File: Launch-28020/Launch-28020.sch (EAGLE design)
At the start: 24 parts, among them U1 3.3V

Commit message: Updated Schematic
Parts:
- removed C2, C3, C4, C5, C6: (no value), rcl:C-USC1206
- removed R4, R6, R7: (no value), resistor:R-US_M1206
- added QF1: 8M10AHC49T, crystal:8M10AHC49T
- R1: value (none) -> 2k2
- R2, R3: value (none) -> 56k
- R8, R9: value (none) -> 4k7
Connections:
- new net N$12: R3.2, U$1.GPIO34
- new net N$6: C8.2, QF1.1, U$1.X1
- new net N$7: C1.2, QF1.3, U$1.X2
- new net N$8: J3.14, R9.1
- new net N$9: J3.13, R8.2
- new net TRST: J3.2, R1.1, U$1.TRST
- net GND: now also C1.1, C8.1, C9.2, J3.10, J3.12, J3.4, J3.8, R1.2, U1.NC
- net TCK: now also J3.11
- net TDI: now also J3.3
- net TDO: now also J3.7, R2.2
- net TMS: now also J3.1
- net VDD: now also C9.1, J3.5, R2.1, R3.1, R8.1, R9.2, U1.OUT
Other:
- moved on the sheet: C1, C11, C8, C9, J3, R1, R2, R3, R8, R9

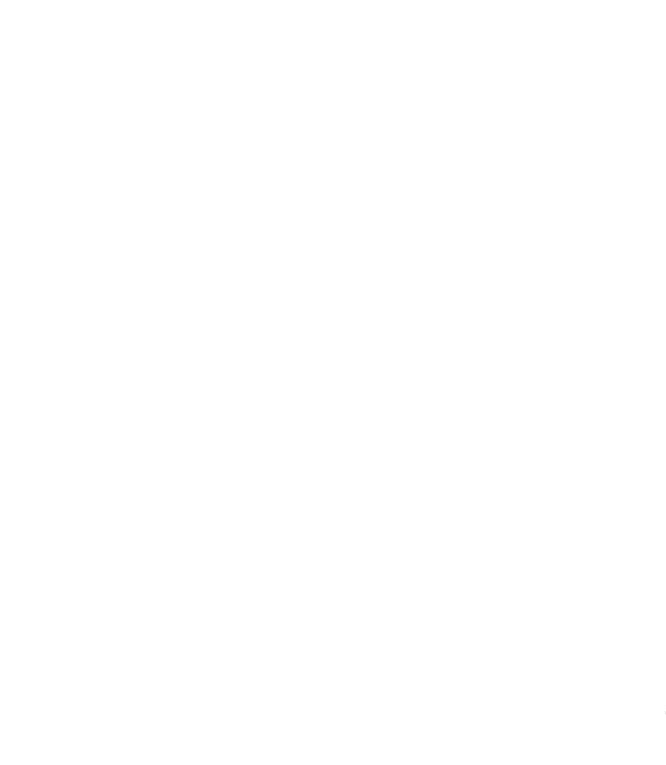
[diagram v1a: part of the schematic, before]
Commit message: Added IO headeres
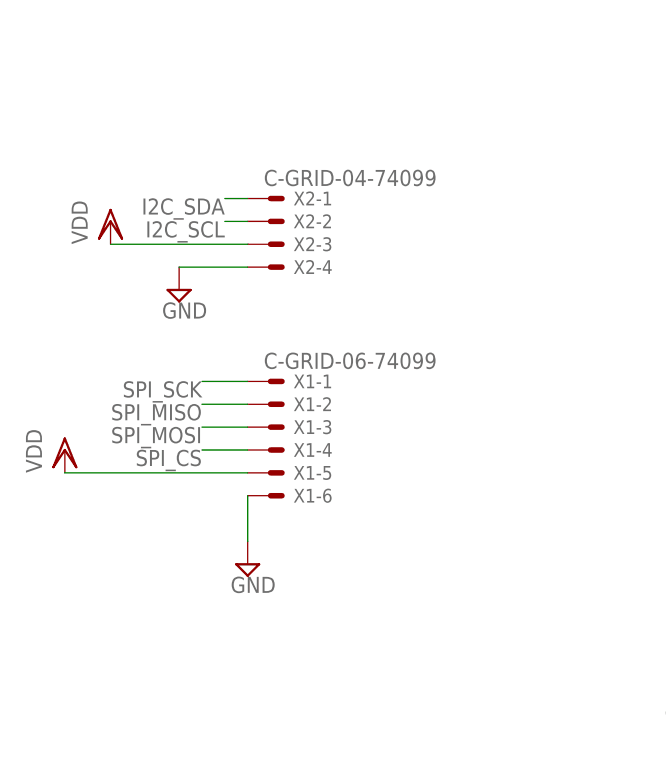
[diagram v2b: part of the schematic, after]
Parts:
- added X1: C-GRID-06-74099, con-molex:C-GRID-06-74099
- added X2: C-GRID-04-74099, con-molex:C-GRID-04-74099
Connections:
- new net I2C_SCL: X2-2.S
- new net I2C_SDA: X2-1.S
- new net SPI_CS: X1-4.S
- new net SPI_MISO: X1-2.S
- new net SPI_MOSI: X1-3.S
- new net SPI_SCK: X1-1.S
- net GND: now also X1-6.S, X2-4.S
- net VDD: now also X1-5.S, X2-3.S
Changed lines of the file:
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@@
 <part name="VDD6" library="supply1" library_urn="urn:adsk.eagle:library:371" deviceset="VDD" device=""/>
 <part name="VDD7" library="supply1" library_urn="urn:adsk.eagle:library:371" deviceset="VDD" device=""/>
+<part name="X1" library="con-molex" library_urn="urn:adsk.eagle:library:165" deviceset="C-GRID-06" device="-74099"/>
+<part name="SUPPLY6" library="supply2" library_urn="urn:adsk.eagle:library:372" deviceset="GND" device=""/>
+<part name="VDD8" library="supply1" library_urn="urn:adsk.eagle:library:371" deviceset="VDD" device=""/>
+<part name="X2" library="con-molex" library_urn="urn:adsk.eagle:library:165" deviceset="C-GRID-04" device="-74099"/>
+<part name="VDD9" library="supply1" library_urn="urn:adsk.eagle:library:371" deviceset="VDD" device=""/>
+<part name="SUPPLY10" library="supply2" library_urn="urn:adsk.eagle:library:372" deviceset="GND" device=""/>
 </parts>
 <sheets>
@@
 <instance part="VDD6" gate="G$1" x="121.92" y="78.74"/>
 <instance part="VDD7" gate="G$1" x="-60.96" y="-33.02" rot="R180"/>
+<instance part="X1" gate="-1" x="-106.68" y="63.5"/>
+<instance part="X1" gate="-2" x="-106.68" y="60.96"/>
+<instance part="X1" gate="-3" x="-106.68" y="58.42"/>
+<instance part="X1" gate="-4" x="-106.68" y="55.88"/>
+<instance part="X1" gate="-5" x="-106.68" y="53.34"/>
+<instance part="X1" gate="-6" x="-106.68" y="50.8"/>
+<instance part="SUPPLY6" gate="GND" x="-109.22" y="43.18"/>
+<instance part="VDD8" gate="G$1" x="-129.54" y="55.88"/>
+<instance part="X2" gate="-1" x="-106.68" y="83.82"/>
+<instance part="X2" gate="-2" x="-106.68" y="81.28"/>
+<instance part="X2" gate="-3" x="-106.68" y="78.74"/>
+<instance part="X2" gate="-4" x="-106.68" y="76.2"/>
+<instance part="VDD9" gate="G$1" x="-124.46" y="81.28"/>
+<instance part="SUPPLY10" gate="GND" x="-116.84" y="73.66"/>
 </instances>
 <busses>
@@
 <wire x1="-60.96" y1="-25.4" x2="-48.26" y2="-25.4" width="0.1524" layer="91"/>
 <pinref part="VDD7" gate="G$1" pin="VDD"/>
+</segment>
+<segment>
+<pinref part="X1" gate="-5" pin="S"/>
+<pinref part="VDD8" gate="G$1" pin="VDD"/>
+<wire x1="-109.22" y1="53.34" x2="-129.54" y2="53.34" width="0.1524" layer="91"/>
+</segment>
+<segment>
+<pinref part="X2" gate="-3" pin="S"/>
+<pinref part="VDD9" gate="G$1" pin="VDD"/>
+<wire x1="-109.22" y1="78.74" x2="-124.46" y2="78.74" width="0.1524" layer="91"/>
 </segment>
 </net>
@@
 <wire x1="63.5" y1="-10.16" x2="63.5" y2="-7.62" width="0.1524" layer="91"/>
 </segment>
+<segment>
+<pinref part="SUPPLY6" gate="GND" pin="GND"/>
+<pinref part="X1" gate="-6" pin="S"/>
+<wire x1="-109.22" y1="45.72" x2="-109.22" y2="50.8" width="0.1524" layer="91"/>
+</segment>
+<segment>
+<pinref part="X2" gate="-4" pin="S"/>
+<pinref part="SUPPLY10" gate="GND" pin="GND"/>
+<wire x1="-109.22" y1="76.2" x2="-116.84" y2="76.2" width="0.1524" layer="91"/>
+</segment>
 </net>
 <net name="N$3" class="0">
@@
 </segment>
 </net>
+<net name="SPI_SCK" class="0">
+<segment>
+<pinref part="X1" gate="-1" pin="S"/>
+<wire x1="-109.22" y1="63.5" x2="-114.3" y2="63.5" width="0.1524" layer="91"/>
+<label x="-114.3" y="63.5" size="1.778" layer="95" rot="R180"/>
+</segment>
+</net>
+<net name="SPI_MISO" class="0">
+<segment>
+<pinref part="X1" gate="-2" pin="S"/>
+<wire x1="-109.22" y1="60.96" x2="-114.3" y2="60.96" width="0.1524" layer="91"/>
+<label x="-114.3" y="60.96" size="1.778" layer="95" rot="R180"/>
+</segment>
+</net>
+<net name="SPI_MOSI" class="0">
+<segment>
+<pinref part="X1" gate="-3" pin="S"/>
+<wire x1="-109.22" y1="58.42" x2="-114.3" y2="58.42" width="0.1524" layer="91"/>
+<label x="-114.3" y="58.42" size="1.778" layer="95" rot="R180"/>
+</segment>
+</net>
+<net name="SPI_CS" class="0">
+<segment>
+<pinref part="X1" gate="-4" pin="S"/>
+<wire x1="-109.22" y1="55.88" x2="-114.3" y2="55.88" width="0.1524" layer="91"/>
+<label x="-114.3" y="55.88" size="1.778" layer="95" rot="R180"/>
+</segment>
+</net>
+<net name="I2C_SDA" class="0">
+<segment>
+<pinref part="X2" gate="-1" pin="S"/>
+<wire x1="-109.22" y1="83.82" x2="-111.76" y2="83.82" width="0.1524" layer="91"/>
+<label x="-111.76" y="83.82" size="1.778" layer="95" rot="R180"/>
+</segment>
+</net>
+<net name="I2C_SCL" class="0">
+<segment>
+<pinref part="X2" gate="-2" pin="S"/>
+<wire x1="-109.22" y1="81.28" x2="-111.76" y2="81.28" width="0.1524" layer="91"/>
+<label x="-111.76" y="81.28" size="1.778" layer="95" rot="R180"/>
+</segment>
+</net>

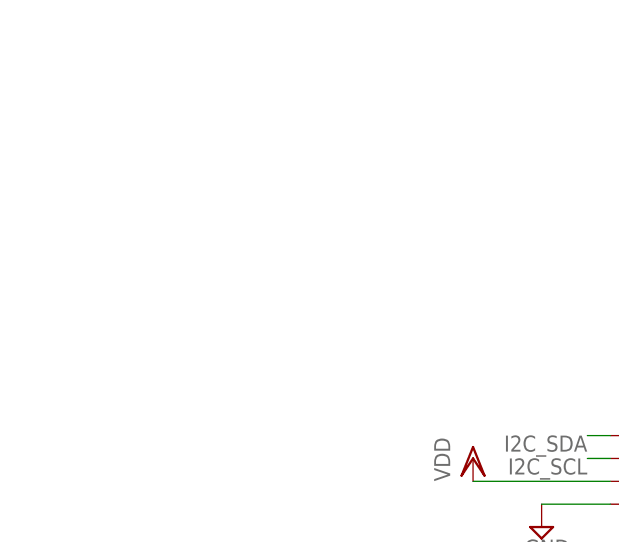
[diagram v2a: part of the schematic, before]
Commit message: Updated the schematic to include power circuitry and connectivity.
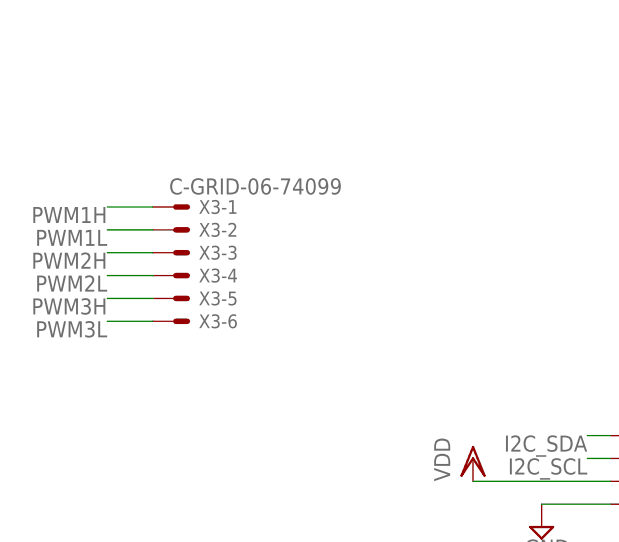
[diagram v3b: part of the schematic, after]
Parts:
- added X3: C-GRID-06-74099, con-molex:C-GRID-06-74099
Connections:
- new net PWM1H: X3-1.S
- new net PWM1L: X3-2.S
- new net PWM2H: X3-3.S
- new net PWM2L: X3-4.S
- new net PWM3H: X3-5.S
- new net PWM3L: X3-6.S
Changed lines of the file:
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@@
 <part name="VDD9" library="supply1" library_urn="urn:adsk.eagle:library:371" deviceset="VDD" device=""/>
 <part name="SUPPLY10" library="supply2" library_urn="urn:adsk.eagle:library:372" deviceset="GND" device=""/>
+<part name="X3" library="con-molex" library_urn="urn:adsk.eagle:library:165" deviceset="C-GRID-06" device="-74099"/>
 </parts>
 <sheets>
@@
 <instance part="VDD9" gate="G$1" x="-124.46" y="81.28"/>
 <instance part="SUPPLY10" gate="GND" x="-116.84" y="73.66"/>
+<instance part="X3" gate="-1" x="-157.48" y="109.22"/>
+<instance part="X3" gate="-2" x="-157.48" y="106.68"/>
+<instance part="X3" gate="-3" x="-157.48" y="104.14"/>
+<instance part="X3" gate="-4" x="-157.48" y="101.6"/>
+<instance part="X3" gate="-5" x="-157.48" y="99.06"/>
+<instance part="X3" gate="-6" x="-157.48" y="96.52"/>
 </instances>
 <busses>
@@
 </segment>
 </net>
+<net name="PWM1H" class="0">
+<segment>
+<pinref part="X3" gate="-1" pin="S"/>
+<wire x1="-160.02" y1="109.22" x2="-165.1" y2="109.22" width="0.1524" layer="91"/>
+<label x="-165.1" y="109.22" size="1.778" layer="95" rot="R180"/>
+</segment>
+</net>
+<net name="PWM1L" class="0">
+<segment>
+<pinref part="X3" gate="-2" pin="S"/>
+<wire x1="-160.02" y1="106.68" x2="-165.1" y2="106.68" width="0.1524" layer="91"/>
+<label x="-165.1" y="106.68" size="1.778" layer="95" rot="R180"/>
+</segment>
+</net>
+<net name="PWM2H" class="0">
+<segment>
+<pinref part="X3" gate="-3" pin="S"/>
+<wire x1="-160.02" y1="104.14" x2="-165.1" y2="104.14" width="0.1524" layer="91"/>
+<label x="-165.1" y="104.14" size="1.778" layer="95" rot="R180"/>
+</segment>
+</net>
+<net name="PWM2L" class="0">
+<segment>
+<pinref part="X3" gate="-4" pin="S"/>
+<wire x1="-160.02" y1="101.6" x2="-165.1" y2="101.6" width="0.1524" layer="91"/>
+<label x="-165.1" y="101.6" size="1.778" layer="95" rot="R180"/>
+</segment>
+</net>
+<net name="PWM3H" class="0">
+<segment>
+<pinref part="X3" gate="-5" pin="S"/>
+<wire x1="-160.02" y1="99.06" x2="-165.1" y2="99.06" width="0.1524" layer="91"/>
+<label x="-165.1" y="99.06" size="1.778" layer="95" rot="R180"/>
+</segment>
+</net>
+<net name="PWM3L" class="0">
+<segment>
+<pinref part="X3" gate="-6" pin="S"/>
+<wire x1="-160.02" y1="96.52" x2="-165.1" y2="96.52" width="0.1524" layer="91"/>
+<label x="-165.1" y="96.52" size="1.778" layer="95" rot="R180"/>
+</segment>
+</net>

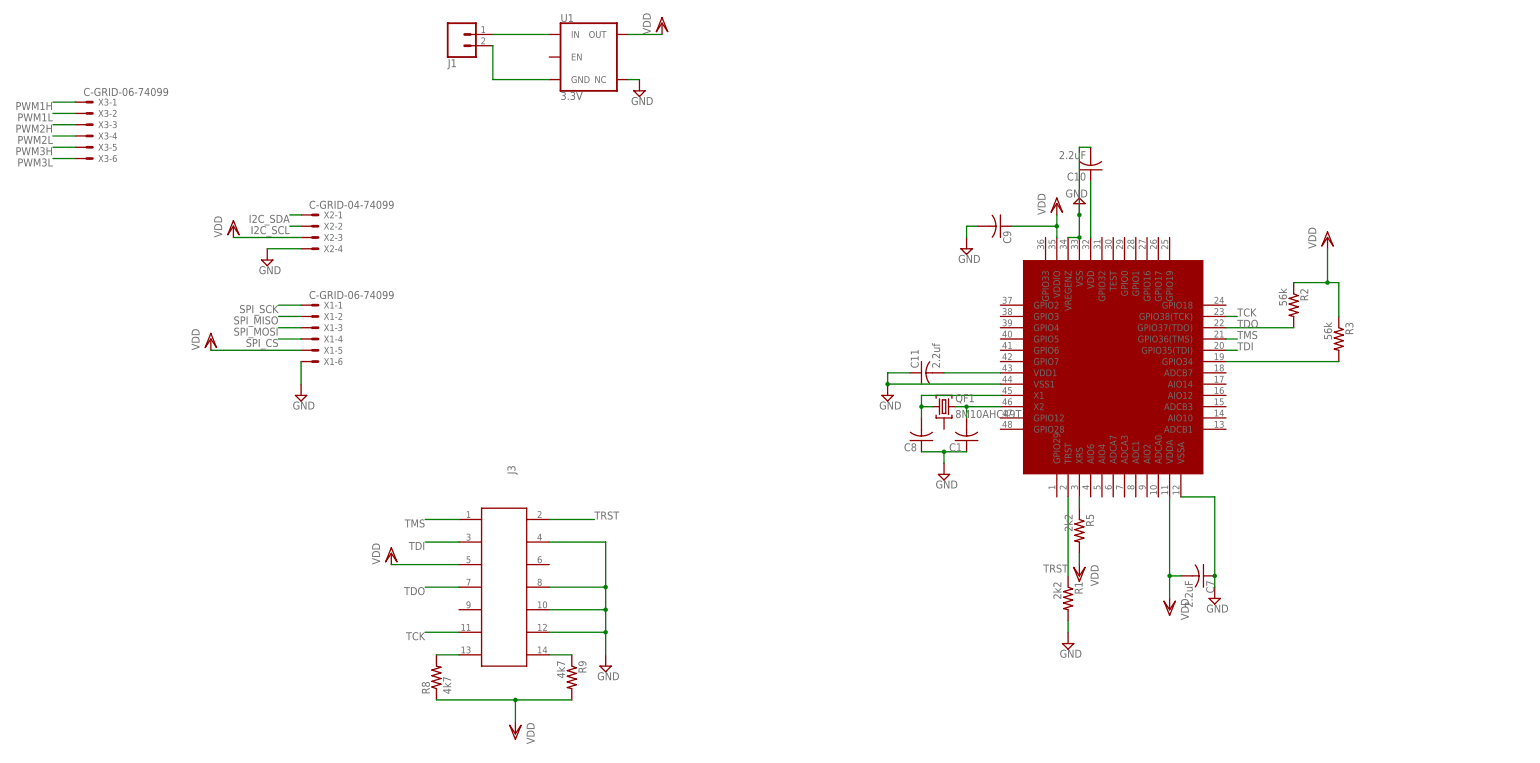
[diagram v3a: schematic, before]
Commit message: Created a working schematic and board layout. THe laytout can be optimized there seens to be some extra board space for the ground plane. Could also use mounting holes.
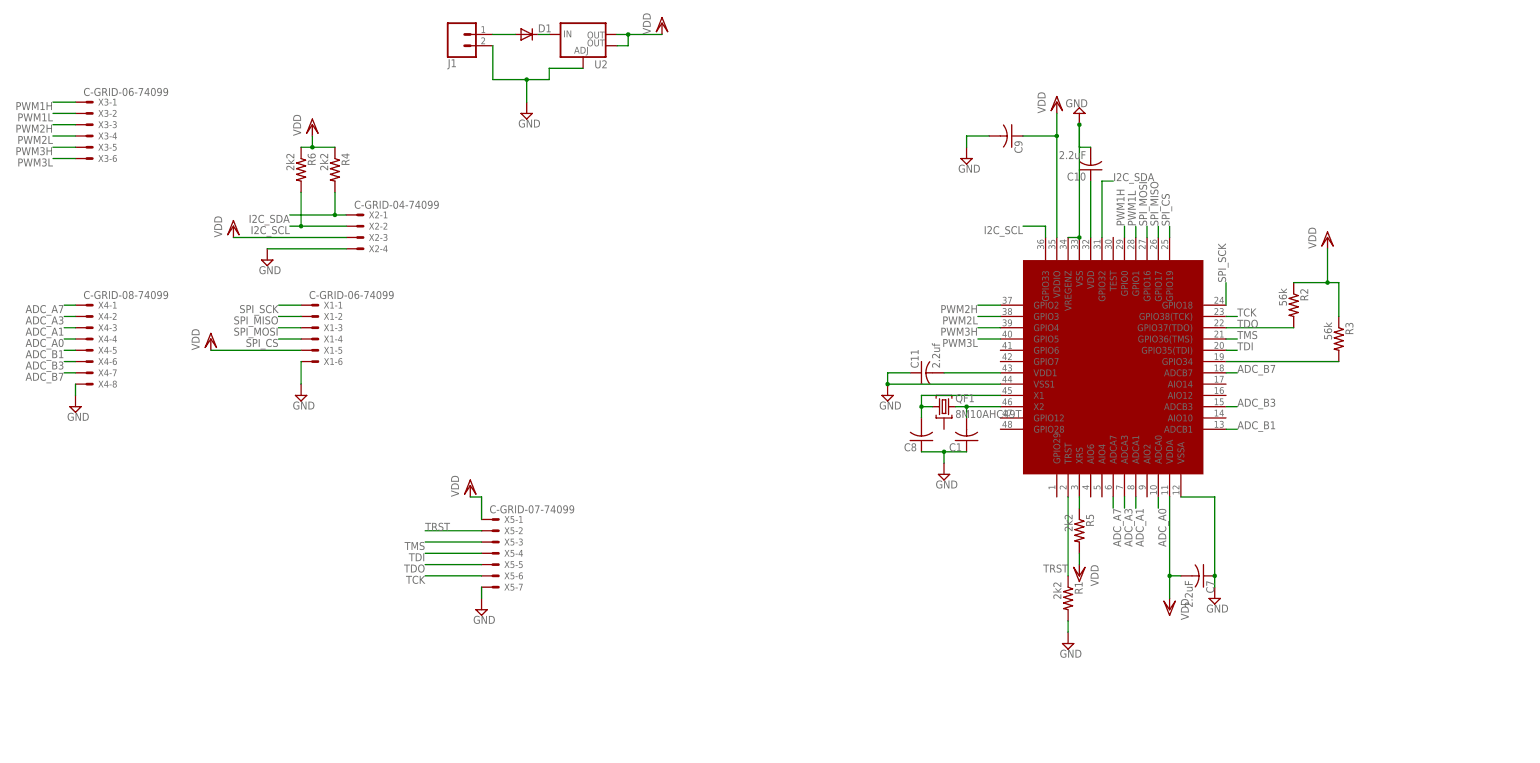
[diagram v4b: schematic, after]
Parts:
- removed J3: (no value), Wurth_Elektronik_Electromechanic_Wire_to_Board_Connectors_rev17b:61201422323
- removed R8, R9: 4k7, resistor:R-US_M1206
- removed U1: 3.3V, SparkFun-IC-Power:V_REG_AP2112K-3.3V
- added D1: (no value), diode:DIODE-SOD106-W
- added R4, R6: 2k2, resistor:R-US_M1206
- added U2: (no value), SparkFun-IC-Power:V_REG_LM1117SOT223
- added X4: C-GRID-08-74099, con-molex:C-GRID-08-74099
- added X5: C-GRID-07-74099, con-molex:C-GRID-07-74099
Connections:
- removed net N$2: J1.2, U1.GND
- removed net N$9: J3.13, R8.2
- new net ADC_A0: U$1.ADCA0, X4-4.S
- new net ADC_A1: U$1.ADCA1, X4-3.S
- new net ADC_A3: U$1.ADCA3, X4-2.S
- new net ADC_A7: U$1.ADCA7, X4-1.S
- new net ADC_B1: U$1.ADCB1, X4-5.S
- new net ADC_B3: U$1.ADCB3, X4-6.S
- new net ADC_B7: U$1.ADCB7, X4-7.S
- net GND: now also J1.2, U2.ADJ, X4-8.S, X5-7.S; no longer J3.10, J3.12, J3.4, J3.8, U1.NC
- net I2C_SCL: now also R6.2, U$1.GPIO33
- net I2C_SDA: now also R4.2, U$1.GPIO32
- net N$1: now also D1.A; no longer U1.IN
- net N$8: now also D1.C, U2.IN; no longer J3.14, R9.1
- net PWM1H: now also U$1.GPIO0
- net PWM1L: now also U$1.GPIO1
- net PWM2H: now also U$1.GPIO2
- net PWM2L: now also U$1.GPIO3
- net PWM3H: now also U$1.GPIO4
- net PWM3L: now also U$1.GPIO5
- net SPI_CS: now also U$1.GPIO19
- net SPI_MISO: now also U$1.GPIO17
- net SPI_MOSI: now also U$1.GPIO16
- net SPI_SCK: now also U$1.GPIO18
- net TCK: now also X5-6.S; no longer J3.11
- net TDI: now also X5-4.S; no longer J3.3
- net TDO: now also X5-5.S; no longer J3.7
- net TMS: now also X5-3.S; no longer J3.1
- net TRST: now also X5-2.S; no longer J3.2
- net VDD: now also R4.1, R6.1, U2.OUT, U2.OUT@1, X5-1.S; no longer J3.5, R8.1, R9.2, U1.OUT
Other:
- moved on the sheet: C9, X2-1, X2-2, X2-3, X2-4
